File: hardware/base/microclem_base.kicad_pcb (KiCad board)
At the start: 2 copper layers, 160 x 100 mm, 61 parts, among them U1 74AHC02, U12 74AHC14, U13 74AHC08, U14 74AHC32, U15 74HC590, U16 74AC163, U17 74AC163, U18 74AHCT245, U19 74HC590, U2 74AHC74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

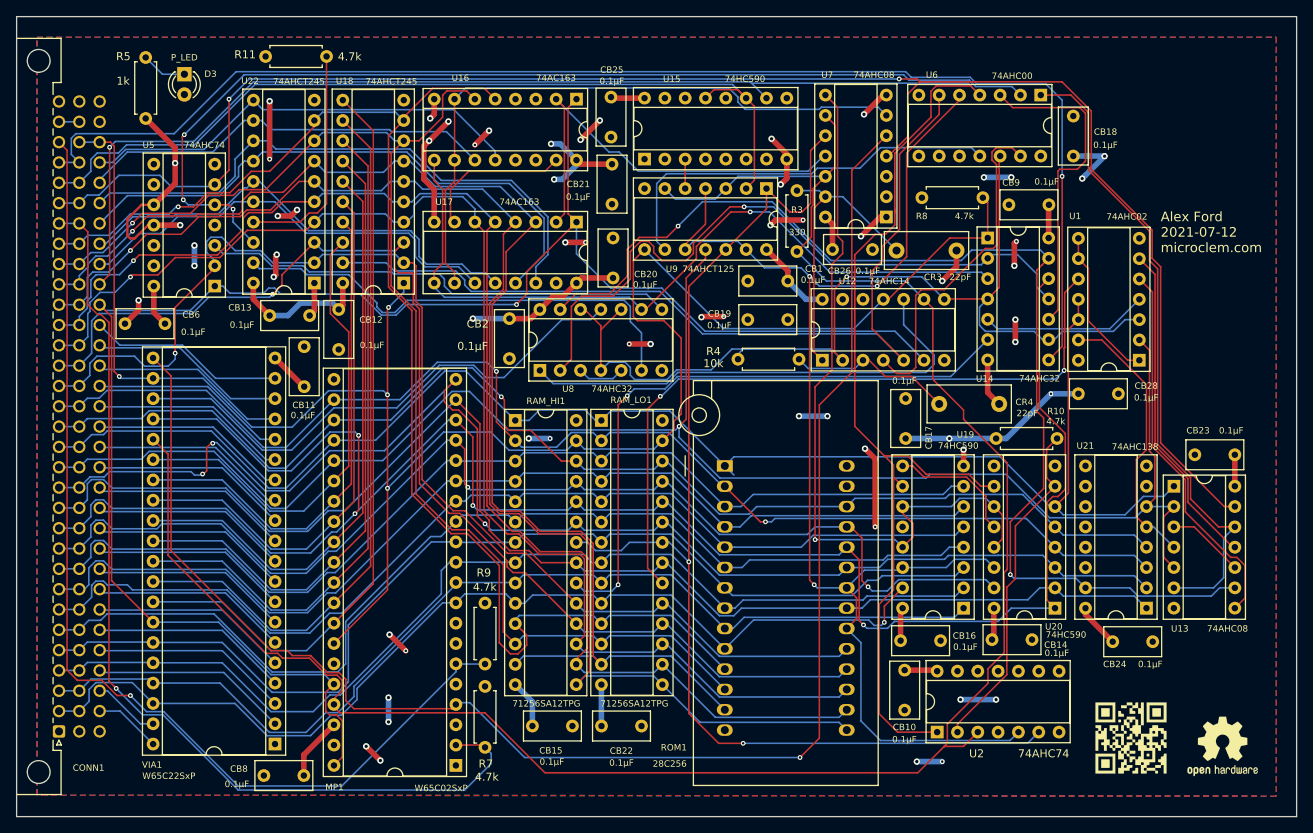
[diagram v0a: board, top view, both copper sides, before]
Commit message: base: mounting holes
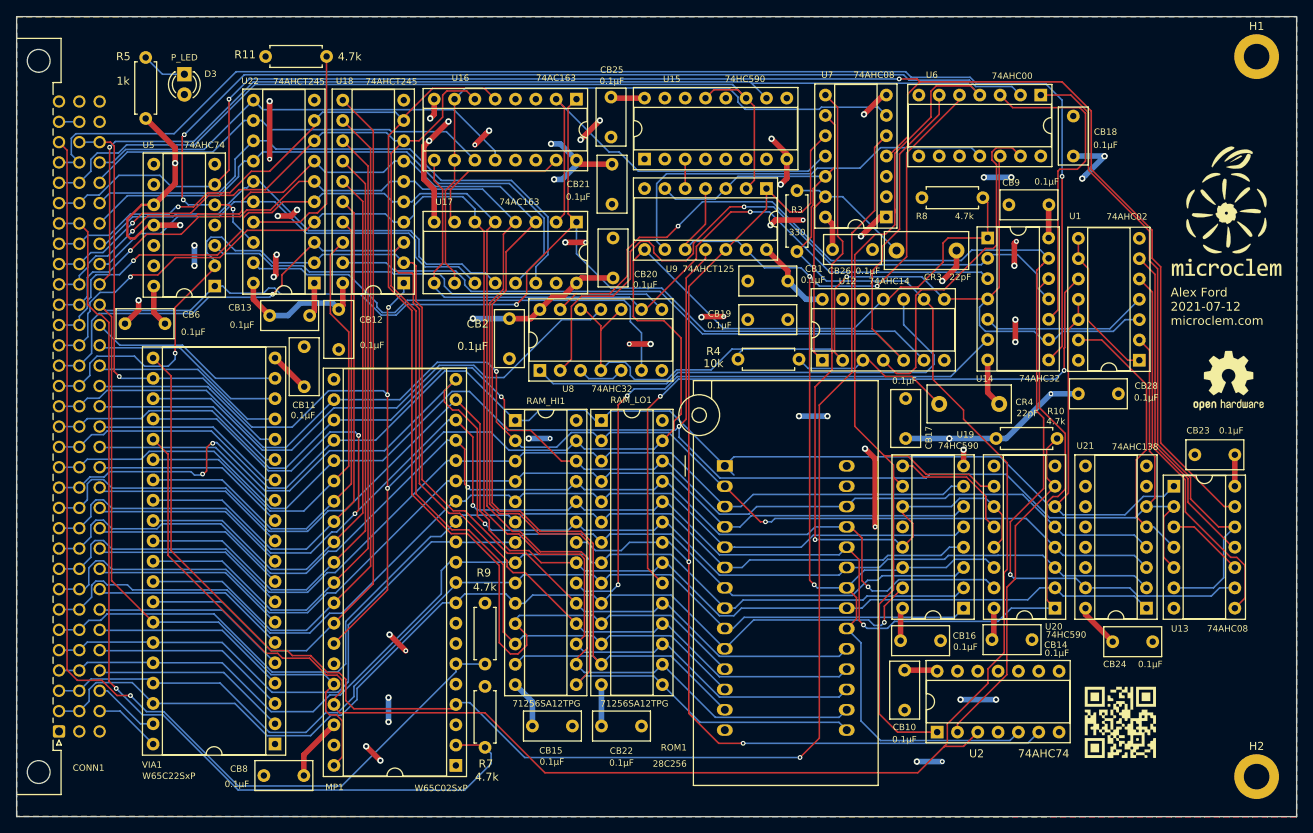
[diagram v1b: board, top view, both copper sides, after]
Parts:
- added G***: LOGO, graphics:microclem_logo_silk_screen, F.Cu at (173.8, 46.7)
- added H1: MountingHole, MountingHole:MountingHole_3.2mm_M3_DIN965_Pad, F.Cu at (177.6, 27.2)
- added H2: MountingHole, MountingHole:MountingHole_3.2mm_M3_DIN965_Pad, F.Cu at (177.6, 117.2)
- LOGO1: moved to B.Cu
- moved LOGO3 45.7 mm to (174.1, 67.7)
- moved LOGO1 12.3 mm to (173.3, 46.7), turned to 180 degrees
- moved LOGO2 2.36 mm to (160.6, 110.4)
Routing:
- net R~W~: track 247.0 -> 248.4 mm
